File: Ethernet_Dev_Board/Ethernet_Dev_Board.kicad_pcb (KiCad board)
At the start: 4 copper layers, 79.9 x 65.2 mm, 116 parts, among them J101 Power In, J401 TAG-CONNECT_NL_10-POS_LEGS, Q201 PMV48XPA2R, U101 AZ1117, U102 74AUP1T08GWH, U103 1.2V, U201 WIZNET_W5500, U402 ESP32-WROOM-32E, U403 74LVC1G11W6, Y201 25MHz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

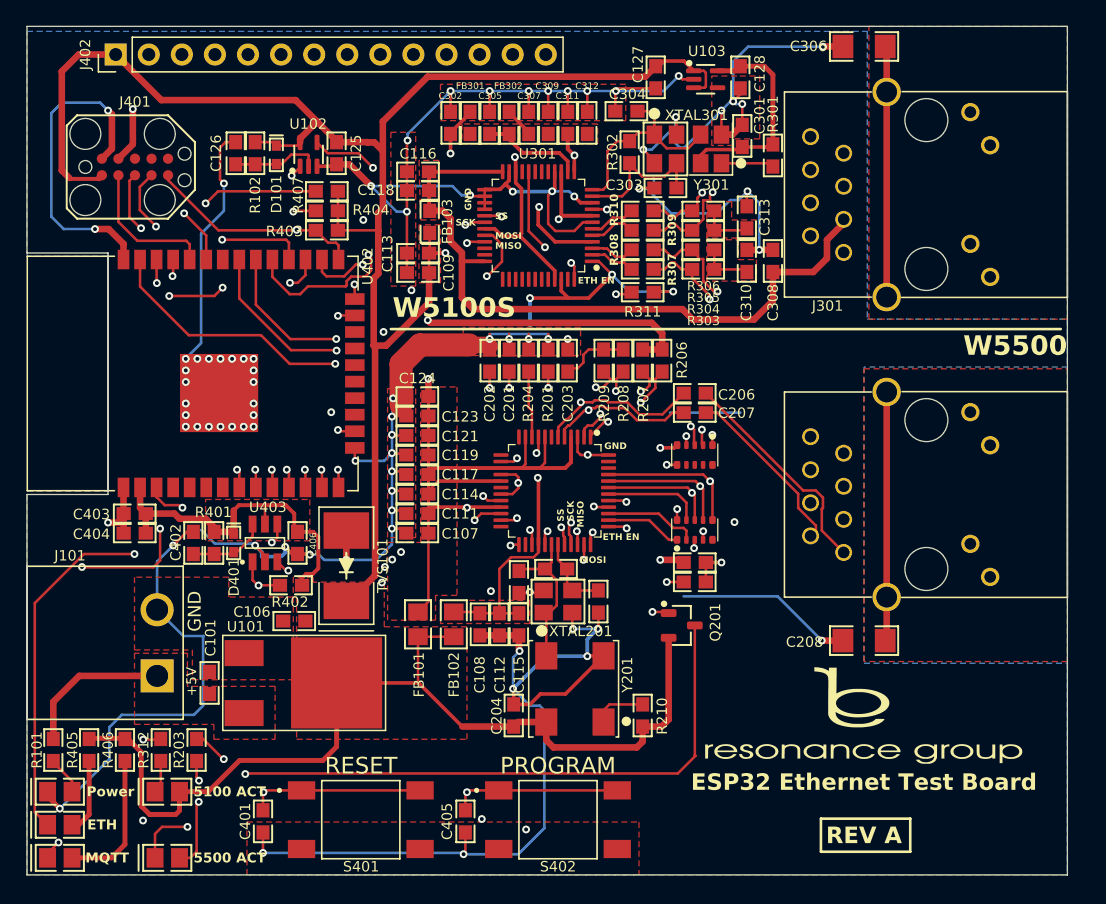
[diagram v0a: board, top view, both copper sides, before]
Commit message: Fixed an issue with a footprint that had height and width of 0,0
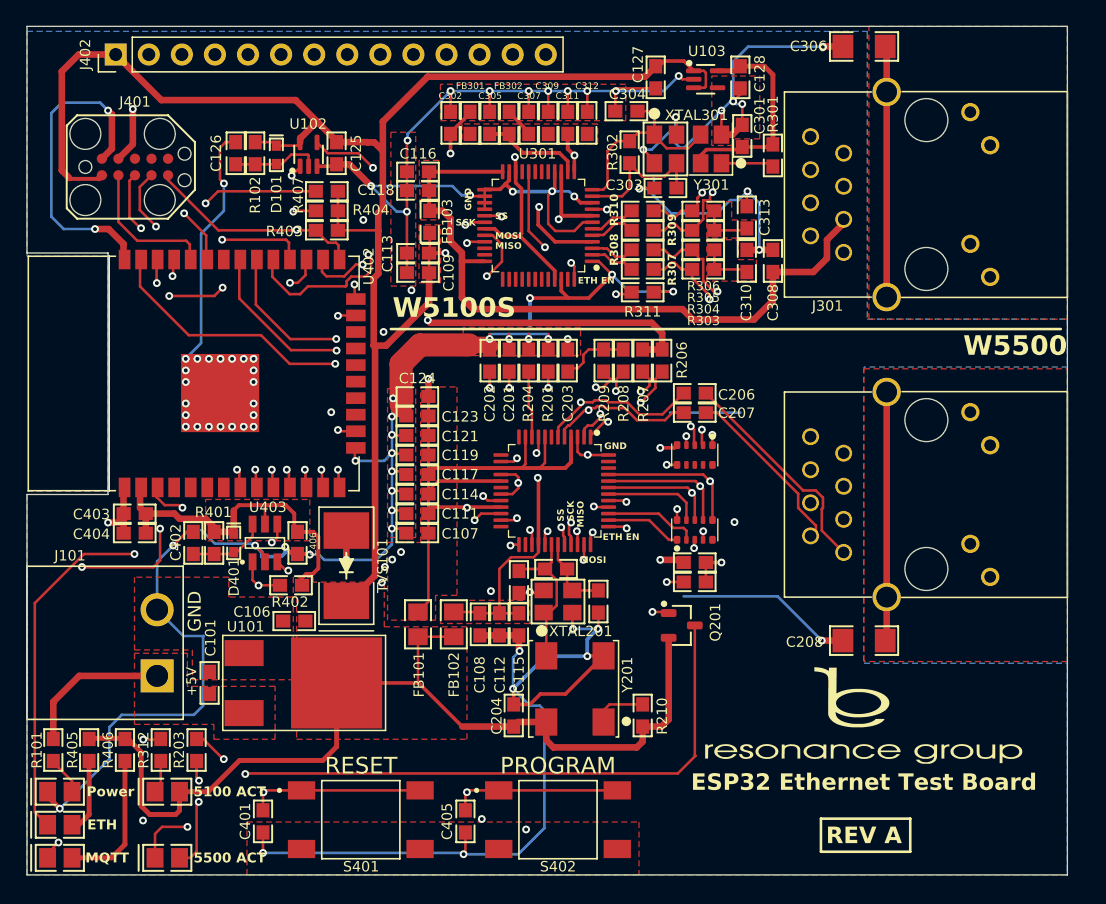
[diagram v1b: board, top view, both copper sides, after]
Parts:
- moved U402 0.08 mm to (84.3, 81.0)
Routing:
- net GND1: track 416.4 -> 412.5 mm
- net +3.3V: track 249.5 -> 248.5 mm
- net Net-(U402-IO22): track 50.5 -> 50.0 mm
